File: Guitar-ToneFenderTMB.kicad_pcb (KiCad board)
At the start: 2 copper layers, 53 x 35 mm, 13 parts, among them J1 Screw_Terminal_1x02, J2 Screw_Terminal_1x02, J3 Screw_Terminal_1x01

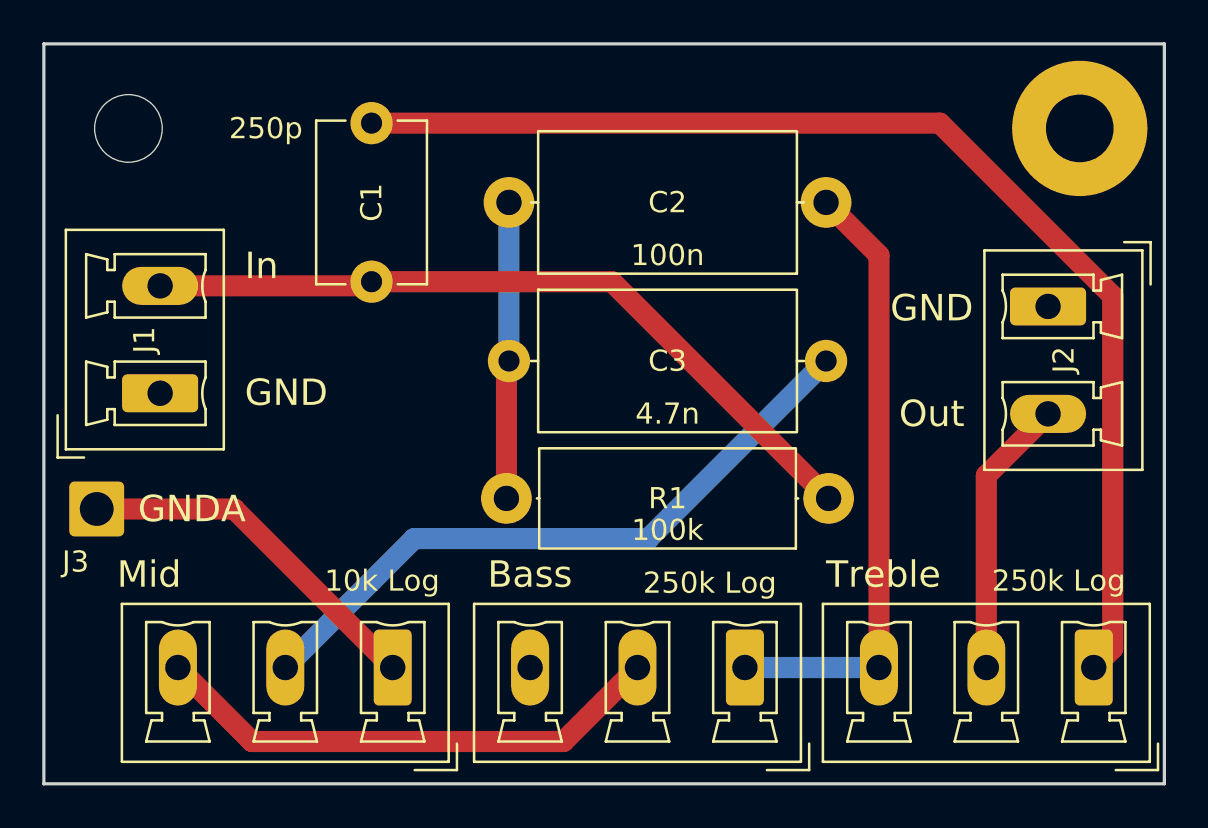
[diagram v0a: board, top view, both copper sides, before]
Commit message: Fixed C3 value to 47n
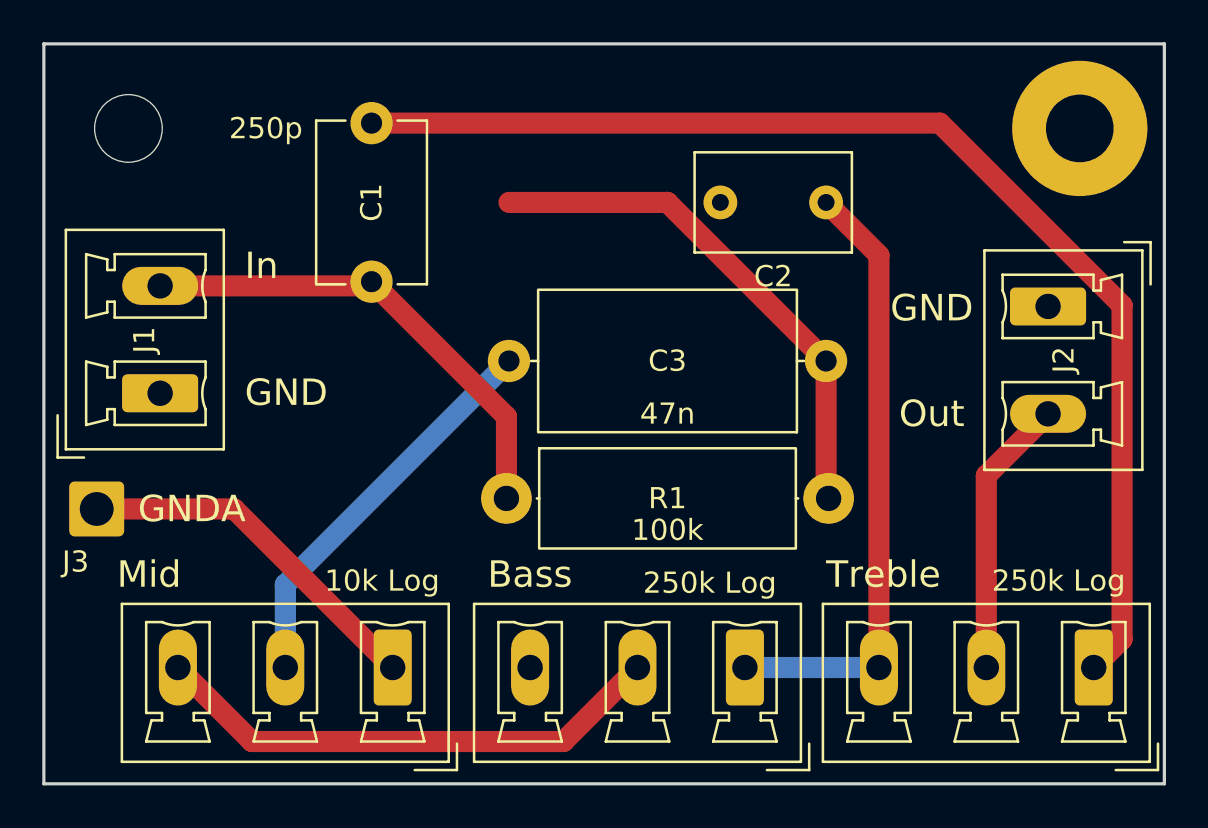
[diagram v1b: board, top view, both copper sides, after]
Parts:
- C2: footprint Local:C_Axial_L12.0mm_D6.5mm_P15.00mm_Horizontal -> Capacitor_THT:C_Rect_L7.2mm_W4.5mm_P5.00mm_FKS2_FKP2_MKS2_MKP2
- C3: value 4.7n -> 47n
- moved R1 15.2 mm to (181.9, 118.5), turned to 0 degrees
- moved C3 15.0 mm to (197.0, 112.0), turned to 180 degrees
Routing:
- net Net-(C1-Pad1): track 35.9 -> 23.0 mm
- net Net-(C3-Pad2): track 31.6 -> 19.1 mm
- net Net-(C2-Pad2): track 14.0 -> 24.7 mm
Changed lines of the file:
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@@
 	(footprint "Resistor_THT:R_Axial_DIN0414_L11.9mm_D4.5mm_P15.24mm_Horizontal"
 		(layer "F.Cu")
-		(at 197.12 118.5 180)
+		(at 181.88 118.5)
 		(descr "Resistor, Axial_DIN0414 series, Axial, Horizontal, pin pitch=15.24mm, 2W, length*diameter=11.9*4.5mm^2, http://www.vishay.com/docs/20128/wkxwrx.pdf")
 		(tags "Resistor Axial_DIN0414 series Axial Horizontal pin pitch 15.24mm 2W length 11.9mm diameter 4.5mm")
@@
 		)
 		(property "Value" "100k"
-			(at 7.62 -1.5 0)
+			(at 7.62 1.5 0)
 			(layer "F.SilkS")
 			(effects
@@
 		)
 		(property "Datasheet" ""
-			(at 0 0 180)
+			(at 0 0 0)
 			(unlocked yes)
 			(layer "F.Fab")
@@
 		)
 		(property "Description" ""
-			(at 0 0 180)
+			(at 0 0 0)
 			(unlocked yes)
 			(layer "F.Fab")
@@
 		)
 		(property "MFR" ""
-			(at 0 0 180)
+			(at 0 0 0)
 			(unlocked yes)
 			(layer "F.Fab")
@@
 		)
 		(property "MPN" ""
-			(at 0 0 180)
+			(at 0 0 0)
 			(unlocked yes)
 			(layer "F.Fab")
@@
 		)
 		(property "SPR" ""
-			(at 0 0 180)
+			(at 0 0 0)
 			(unlocked yes)
 			(layer "F.Fab")
@@
 		)
 		(property "SPN" ""
-			(at 0 0 180)
+			(at 0 0 0)
 			(unlocked yes)
 			(layer "F.Fab")
@@
 		)
 		(property "SPURL" ""
-			(at 0 0 180)
+			(at 0 0 0)
 			(unlocked yes)
 			(layer "F.Fab")
@@
 		(attr through_hole)
 		(fp_line
-			(start 13.8 0)
-			(end 13.69 0)
+			(start 1.44 0)
+			(end 1.55 0)
 			(stroke
 				(width 0.12)
@@
 		)
 		(fp_line
-			(start 1.44 0)
-			(end 1.55 0)
+			(start 13.8 0)
+			(end 13.69 0)
 			(stroke
 				(width 0.12)
@@
 		)
 		(fp_line
-			(start 15.24 0)
-			(end 13.57 0)
+			(start 0 0)
+			(end 1.67 0)
 			(stroke
 				(width 0.1)
@@
 		)
 		(fp_line
-			(start 0 0)
-			(end 1.67 0)
+			(start 15.24 0)
+			(end 13.57 0)
 			(stroke
 				(width 0.1)
@@
 		)
 		(pad "1" thru_hole circle
-			(at 0 0 180)
+			(at 0 0)
 			(size 2.4 2.4)
 			(drill 1.2)
@@
 		)
 		(pad "2" thru_hole circle
-			(at 15.24 0 180)
+			(at 15.24 0)
 			(size 2.4 2.4)
 			(drill 1.2)
@@
 		)
 	)
-	(footprint "Local:C_Axial_L12.0mm_D6.5mm_P15.00mm_Horizontal"
+	(footprint "Capacitor_THT:C_Rect_L7.2mm_W4.5mm_P5.00mm_FKS2_FKP2_MKS2_MKP2"
 		(layer "F.Cu")
 		(at 197 104.5 180)
-		(descr "C, Axial series, Axial, Horizontal, pin pitch=15mm, length*diameter=12*6.5mm^2, http://cdn-reichelt.de/documents/datenblatt/B300/STYROFLEX.pdf")
-		(tags "C Axial series Axial Horizontal pin pitch 15mm  length 12mm diameter 6.5mm")
+		(descr "C, Rect series, Radial, pin pitch=5.00mm, length*width=7.2*4.5mm^2, Capacitor, http://www.wima.com/EN/WIMA_FKS_2.pdf")
+		(tags "C Rect series Radial pin pitch 5.00mm length 7.2mm width 4.5mm Capacitor")
 		(property "Reference" "C2"
-			(at 7.5 0 180)
+			(at 2.5 -3.5 180)
 			(layer "F.SilkS")
 			(effects
@@
 		)
 		(property "Value" "100n"
-			(at 7.5 -2.5 180)
-			(layer "F.SilkS")
+			(at 2.5 3.5 180)
+			(layer "F.Fab")
 			(effects
 				(font
@@
 		(attr through_hole)
 		(fp_line
-			(start 13.96 0)
-			(end 13.62 0)
+			(start 6.22 2.37)
+			(end -1.22 2.37)
 			(stroke
 				(width 0.12)
@@
 		)
 		(fp_line
-			(start 1.04 0)
-			(end 1.38 0)
+			(start 6.22 -2.37)
+			(end 6.22 2.37)
 			(stroke
 				(width 0.12)
@@
 			(layer "F.SilkS")
 		)
-		(fp_rect
-			(start 1.38 -3.37)
-			(end 13.62 3.37)
+		(fp_line
+			(start -1.22 2.37)
+			(end -1.22 -2.37)
 			(stroke
 				(width 0.12)
 				(type solid)
 			)
-			(fill no)
 			(layer "F.SilkS")
 		)
-		(fp_rect
-			(start -1.55 -3.5)
-			(end 16.55 3.5)
-			(stroke
-				(width 0.05)
-				(type solid)
-			)
-			(fill no)
-			(layer "F.CrtYd")
-		)
 		(fp_line
-			(start 15 0)
-			(end 13.5 0)
+			(start -1.22 -2.37)
+			(end 6.22 -2.37)
 			(stroke
-				(width 0.1)
+				(width 0.12)
 				(type solid)
 			)
-			(layer "F.Fab")
+			(layer "F.SilkS")
 		)
-		(fp_line
-			(start 0 0)
-			(end 1.5 0)
+		(fp_rect
+			(start -1.35 -2.5)
+			(end 6.35 2.5)
 			(stroke
-				(width 0.1)
+				(width 0.05)
 				(type solid)
 			)
-			(layer "F.Fab")
+			(fill no)
+			(layer "F.CrtYd")
 		)
 		(fp_rect
-			(start 1.5 -3.25)
-			(end 13.5 3.25)
+			(start -1.1 -2.25)
+			(end 6.1 2.25)
 			(stroke
 				(width 0.1)
@@
 		)
 		(fp_text user "${REFERENCE}"
-			(at 7.5 0 180)
+			(at 2.5 0 180)
 			(layer "F.Fab")
 			(effects
@@
 		(pad "1" thru_hole circle
 			(at 0 0 180)
-			(size 2.4 2.4)
-			(drill 1.2)
+			(size 1.6 1.6)
+			(drill 0.8)
 			(layers "*.Cu" "*.Mask")
 			(remove_unused_layers no)
@@
 		)
 		(pad "2" thru_hole circle
-			(at 15 0 180)
-			(size 2.4 2.4)
-			(drill 1.2)
+			(at 5 0 180)
+			(size 1.6 1.6)
+			(drill 0.8)
 			(layers "*.Cu" "*.Mask")
 			(remove_unused_layers no)
@@
 		)
 		(embedded_fonts no)
-		(model "${KICAD9_3DMODEL_DIR}/Capacitor_THT.3dshapes/C_Axial_L12.0mm_D6.5mm_P15.00mm_Horizontal.step"
+		(model "${KICAD9_3DMODEL_DIR}/Capacitor_THT.3dshapes/C_Rect_L7.2mm_W4.5mm_P5.00mm_FKS2_FKP2_MKS2_MKP2.step"
 			(offset
 				(xyz 0 0 0)
@@
 	(footprint "Local:C_Axial_L12.0mm_D6.5mm_P15.00mm_Horizontal"
 		(layer "F.Cu")
-		(at 182 112)
+		(at 197 112 180)
 		(descr "C, Axial series, Axial, Horizontal, pin pitch=15mm, length*diameter=12*6.5mm^2, http://cdn-reichelt.de/documents/datenblatt/B300/STYROFLEX.pdf")
 		(tags "C Axial series Axial Horizontal pin pitch 15mm  length 12mm diameter 6.5mm")
@@
 			)
 		)
-		(property "Value" "4.7n"
-			(at 7.5 2.5 0)
+		(property "Value" "47n"
+			(at 7.5 -2.5 0)
 			(layer "F.SilkS")
 			(effects
@@
 		)
 		(property "MFR" ""
-			(at 0 0 0)
+			(at 0 0 180)
 			(unlocked yes)
 			(layer "F.Fab")
@@
 		)
 		(property "MPN" ""
-			(at 0 0 0)
+			(at 0 0 180)
 			(unlocked yes)
 			(layer "F.Fab")
@@
 		)
 		(property "SPR" ""
-			(at 0 0 0)
+			(at 0 0 180)
 			(unlocked yes)
 			(layer "F.Fab")
@@
 		)
 		(property "SPN" ""
-			(at 0 0 0)
+			(at 0 0 180)
 			(unlocked yes)
 			(layer "F.Fab")
@@
 		)
 		(property "SPURL" ""
-			(at 0 0 0)
+			(at 0 0 180)
 			(unlocked yes)
 			(layer "F.Fab")
@@
 		(attr through_hole)
 		(fp_line
-			(start 1.04 0)
-			(end 1.38 0)
+			(start 13.96 0)
+			(end 13.62 0)
 			(stroke
 				(width 0.12)
@@
 		)
 		(fp_line
-			(start 13.96 0)
-			(end 13.62 0)
+			(start 1.04 0)
+			(end 1.38 0)
 			(stroke
 				(width 0.12)
@@
 		)
 		(fp_line
-			(start 0 0)
-			(end 1.5 0)
+			(start 15 0)
+			(end 13.5 0)
 			(stroke
 				(width 0.1)
@@
 		)
 		(fp_line
-			(start 15 0)
-			(end 13.5 0)
+			(start 0 0)
+			(end 1.5 0)
 			(stroke
 				(width 0.1)
@@
 		)
 		(pad "1" thru_hole circle
-			(at 0 0)
+			(at 0 0 180)
 			(size 2 2)
 			(drill 1)
@@
 		)
 		(pad "2" thru_hole circle
-			(at 15 0)
+			(at 15 0 180)
 			(size 2 2)
 			(drill 1)
@@
 	)
 	(segment
-		(start 175.5 108.25)
-		(end 186.87 108.25)
+		(start 181.88 114.63)
+		(end 181.88 118.5)
 		(width 1)
 		(layer "F.Cu")
@@
 	)
 	(segment
-		(start 186.87 108.25)
-		(end 197.12 118.5)
+		(start 165.5 108.4475)
+		(end 175.3025 108.4475)
 		(width 1)
 		(layer "F.Cu")
@@
 	)
 	(segment
-		(start 165.5 108.4475)
-		(end 175.3025 108.4475)
+		(start 175.5 108.25)
+		(end 181.88 114.63)
 		(width 1)
 		(layer "F.Cu")
@@
 	)
 	(segment
-		(start 202.381844 100.75)
-		(end 210.56 108.928156)
+		(start 211 109.368156)
+		(end 211 125.16)
 		(width 1)
 		(layer "F.Cu")
@@
 	)
 	(segment
-		(start 210.56 125.6)
+		(start 211 125.16)
 		(end 209.66 126.5)
 		(width 1)
@@
 	)
 	(segment
-		(start 210.56 108.928156)
-		(end 210.56 125.6)
+		(start 202.381844 100.75)
+		(end 211 109.368156)
 		(width 1)
 		(layer "F.Cu")
@@
 	)
 	(segment
-		(start 181.88 112.12)
-		(end 182 112)
+		(start 189.5 104.5)
+		(end 182 104.5)
 		(width 1)
 		(layer "F.Cu")
@@
 	)
 	(segment
-		(start 181.88 118.5)
-		(end 181.88 112.12)
+		(start 197 112)
+		(end 189.5 104.5)
 		(width 1)
 		(layer "F.Cu")
@@
 	)
 	(segment
-		(start 182 104.5)
-		(end 182 112)
+		(start 197 118.38)
+		(end 197.12 118.5)
 		(width 1)
-		(layer "B.Cu")
+		(layer "F.Cu")
+		(net 6)
+	)
+	(segment
+		(start 197 112)
+		(end 197 118.38)
+		(width 1)
+		(layer "F.Cu")
 		(net 6)
 	)
@@
 	)
 	(segment
-		(start 171.42 126.5)
-		(end 177.519 120.401)
+		(start 181.88 112.12)
+		(end 182 112)
 		(width 1)
-		(layer "B.Cu")
+		(layer "F.Cu")
 		(net 8)
 	)
 	(segment
-		(start 177.519 120.401)
-		(end 188.599 120.401)
+		(start 182 112)
+		(end 171.42 122.58)
 		(width 1)
 		(layer "B.Cu")
@@
 	)
 	(segment
-		(start 188.599 120.401)
-		(end 197 112)
+		(start 171.42 122.58)
+		(end 171.42 126.5)
 		(width 1)
 		(layer "B.Cu")
